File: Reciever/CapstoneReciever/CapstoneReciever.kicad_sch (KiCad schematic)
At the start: 44 parts, among them J1 Conn_01x04, Q1 CSD18502Q5B, Q2 CSD18502Q5B, U1 LM73606RNPR, U2 TPS552882RPMR, U3 ESP32-WROOM-32UE

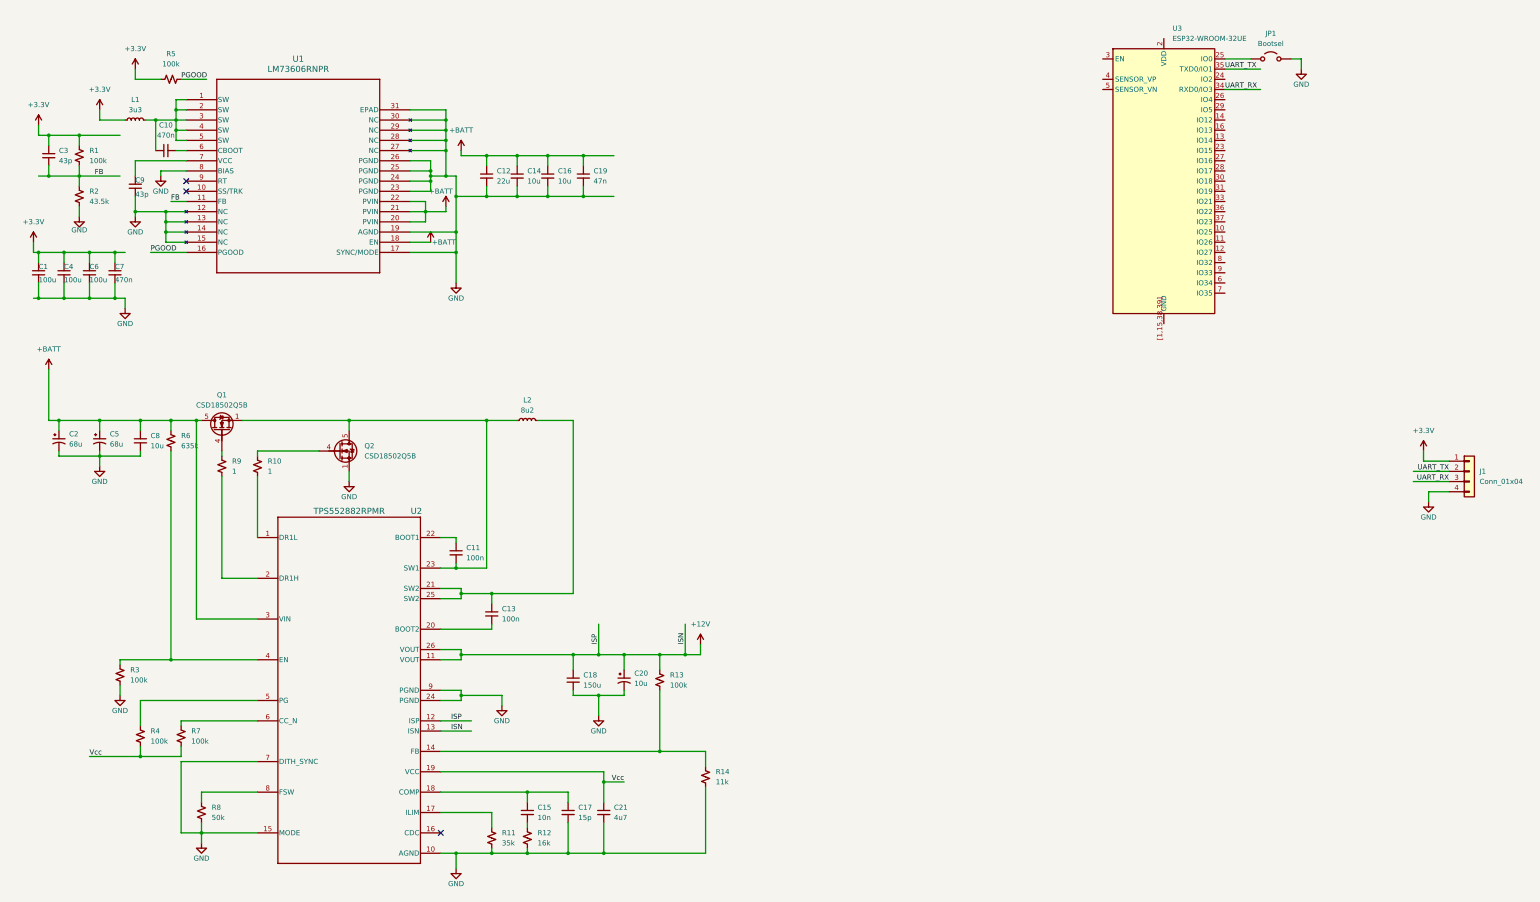
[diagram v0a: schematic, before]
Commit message: Finished ESP32 power and added in solenoid low side switching with TVS for coil transient protection
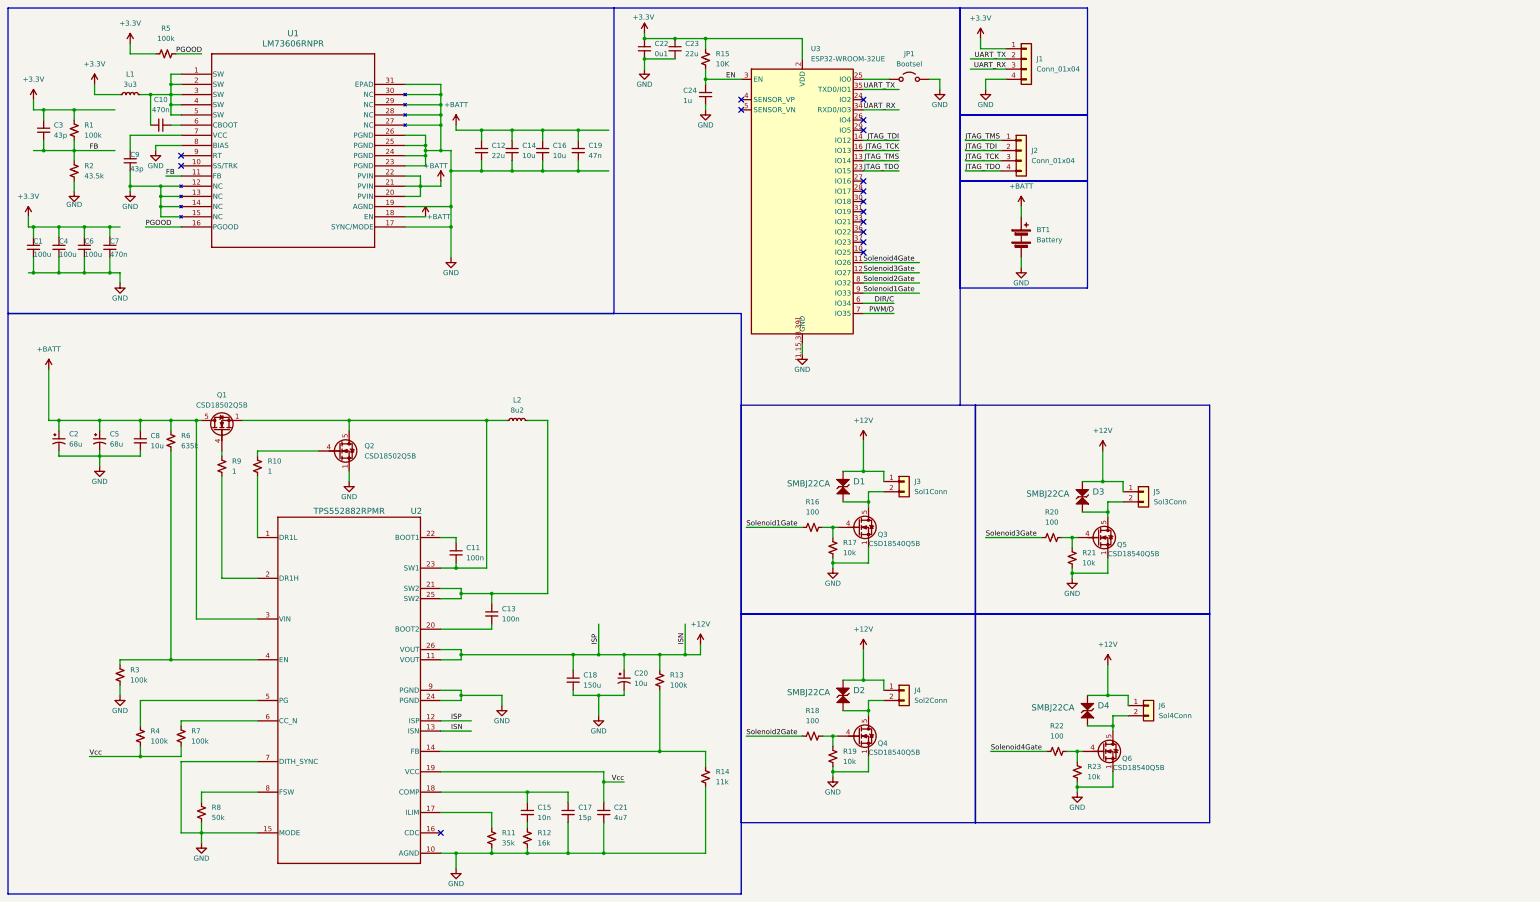
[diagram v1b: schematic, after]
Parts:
- added BT1: Battery, symbol Device:Battery
- added C22: 0u1, symbol Device:C_Small
- added C23: 22u, symbol Device:C_Small
- added C24: 1u, symbol Device:C_Small
- added D1, D2, D3, D4: ${DEVICE}, ICs And Semiconductors SMD:DIOM5336X265N, symbol CERN:Diodes/SMBJ22CA
- added J2: Conn_01x04, symbol Connector_Generic:Conn_01x04
- added J3: Sol1Conn, symbol Connector_Generic:Conn_01x02
- added J4: Sol2Conn, symbol Connector_Generic:Conn_01x02
- added J5: Sol3Conn, symbol Connector_Generic:Conn_01x02
- added J6: Sol4Conn, symbol Connector_Generic:Conn_01x02
- added Q3, Q4, Q5, Q6: CSD18540Q5B, Package_TO_SOT_SMD:TDSON-8-1, symbol Transistor_FET:CSD18540Q5B
- added R15: 10K, symbol Device:R_Small_US
- added R16, R18, R20, R22: 100, symbol Device:R_Small_US
- added R17, R19, R21, R23: 10k, symbol Device:R_Small_US
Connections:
- net +12V: now also D1.2, D2.2, D3.2, D4.2, J3.1 (Pin_1), J4.1 (Pin_1), J5.1 (Pin_1), J6.1 (Pin_1)
- net +3.3V: now also U3.2 (VDD), C22.1, C23.1, R15.1
- net +BATT: now also BT1.1 (+)
- net GND: now also U3.[1,15,38,39] (GND), BT1.2 (-), C22.2, C23.2, C24.2, Q3.1 (S), Q3.2 (S), Q3.3 (S), Q4.1 (S), Q4.2 (S), Q4.3 (S), Q5.1 (S), Q5.2 (S), Q5.3 (S), Q6.1 (S), Q6.2 (S), Q6.3 (S), R17.2, R19.2, R21.2, R23.2
- net Solenoid4Gate: now reaches U3.11 (IO26)
- net Solenoid4Gate: now also R22.1
- net Solenoid3Gate: now reaches U3.12 (IO27)
- net Solenoid3Gate: now also R20.1
- net JTAG_TMS: now reaches U3.13 (IO14)
- net JTAG_TMS: now also J2.1 (Pin_1)
- net JTAG_TDI: now reaches U3.14 (IO12)
- net JTAG_TDI: now also J2.2 (Pin_2)
- net JTAG_TCK: now reaches U3.16 (IO13)
- net JTAG_TCK: now also J2.3 (Pin_3)
- net JTAG_TDO: now reaches U3.23 (IO15)
- net JTAG_TDO: now also J2.4 (Pin_4)
- net EN: now reaches U3.3 (EN)
- net EN: now also C24.1, R15.2
- net DIR/C: now reaches U3.6 (IO34)
- net PWM/D: now reaches U3.7 (IO35)
- net Solenoid2Gate: now reaches U3.8 (IO32)
- net Solenoid2Gate: now also R18.1
- net Solenoid1Gate: now reaches U3.9 (IO33)
- net Solenoid1Gate: now also R16.1
- new net: Q3.4 (G), R16.2, R17.1
- new net: Q4.4 (G), R18.2, R19.1
- new net: D2.1, J4.2 (Pin_2), Q4.5 (D)
- new net: Q6.4 (G), R22.2, R23.1
- new net: D4.1, J6.2 (Pin_2), Q6.5 (D)
- new net: D1.1, J3.2 (Pin_2), Q3.5 (D)
- new net: D3.1, J5.2 (Pin_2), Q5.5 (D)
- new net: Q5.4 (G), R20.2, R21.1
- no-connect marks 3 -> 16
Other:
- moved on the sheet: C1, C10, C12, C14, C16, C19, C3, C4, C6, C7, C9, J1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

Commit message: Assigned footprints to components and moved them into the board editor
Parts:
- BT1, J3, J4, J5, J6: footprint (none) -> TerminalBlock_CUI:TerminalBlock_CUI_TB007-508-02_1x02_P5.08mm_Horizontal
- C1, C12, C14, C16, C18, C2, C20, C21, C23, C24, C4, C5, C6, C8, L1, L2: footprint (none) -> Capacitor_SMD:C_0603_1608Metric
- C10, C11, C13, C15, C17, C19, C22, C3, C7, C9: footprint (none) -> Capacitor_SMD:C_0402_1005Metric
- D1, D2, D3, D4: footprint ICs And Semiconductors SMD:DIOM5336X265N -> Diode_SMD:D_SMB
- J1, J2: footprint (none) -> Connector_PinHeader_2.54mm:PinHeader_1x04_P2.54mm_Vertical
- JP1: footprint (none) -> Connector_PinHeader_2.54mm:PinHeader_1x02_P2.54mm_Vertical
- R1, R10, R11, R12, R13, R14, R15, R16, R17, R18, R19, R2, R20, R21, R22, R23, R3, R4, R5, R6, R7, R8, R9: footprint (none) -> Resistor_SMD:R_0603_1608Metric
- U1: footprint RNP30_TEX -> footprints2:RNP30_TEX
- U2: footprint RPM0026A-MFG -> footprints2:RPM0026A-MFG
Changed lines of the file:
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@@
 			)
 		)
-		(property "Footprint" ""
+		(property "Footprint" "Capacitor_SMD:C_0603_1608Metric"
 			(at 152.4 179.07 0)
 			(hide yes)
@@
 			)
 		)
-		(property "Footprint" ""
+		(property "Footprint" "Resistor_SMD:R_0603_1608Metric"
 			(at 185.42 203.2 0)
 			(hide yes)
@@
 			)
 		)
-		(property "Footprint" ""
+		(property "Footprint" "Capacitor_SMD:C_0402_1005Metric"
 			(at 123.19 147.32 0)
 			(hide yes)
@@
 			)
 		)
-		(property "Footprint" "RNP30_TEX"
+		(property "Footprint" "footprints2:RNP30_TEX"
 			(at 54.61 27.94 0)
 			(hide yes)
@@
 			)
 		)
-		(property "Footprint" "RPM0026A-MFG"
+		(property "Footprint" "footprints2:RPM0026A-MFG"
 			(at 96.52 181.61 0)
 			(hide yes)
@@
 			)
 		)
-		(property "Footprint" ""
+		(property "Footprint" "Connector_PinHeader_2.54mm:PinHeader_1x02_P2.54mm_Vertical"
 			(at 236.22 29.21 0)
 			(hide yes)
@@
 			)
 		)
-		(property "Footprint" ""
+		(property "Footprint" "Resistor_SMD:R_0603_1608Metric"
 			(at 54.61 193.04 0)
 			(hide yes)
@@
 			)
 		)
-		(property "Footprint" ""
+		(property "Footprint" "Capacitor_SMD:C_0402_1005Metric"
 			(at 36.83 71.12 0)
 			(hide yes)
@@
 			)
 		)
-		(property "Footprint" ""
+		(property "Footprint" "Capacitor_SMD:C_0603_1608Metric"
 			(at 160.02 212.09 0)
 			(hide yes)
@@
 			)
 		)
-		(property "Footprint" ""
+		(property "Footprint" "Capacitor_SMD:C_0603_1608Metric"
 			(at 138.43 114.3 0)
 			(hide yes)
@@
 			)
 		)
-		(property "Footprint" ""
+		(property "Footprint" "Resistor_SMD:R_0603_1608Metric"
 			(at 217.17 146.05 0)
 			(hide yes)
@@
 			)
 		)
-		(property "Footprint" ""
+		(property "Footprint" "Capacitor_SMD:C_0603_1608Metric"
 			(at 137.16 46.99 0)
 			(hide yes)
@@
 			)
 		)
-		(property "Footprint" ""
+		(property "Footprint" "Resistor_SMD:R_0603_1608Metric"
 			(at 52.07 119.38 0)
 			(hide yes)
@@
 			)
 		)
-		(property "Footprint" ""
+		(property "Footprint" "Capacitor_SMD:C_0603_1608Metric"
 			(at 129.54 46.99 0)
 			(hide yes)
@@
 			)
 		)
-		(property "Footprint" ""
+		(property "Footprint" "TerminalBlock_CUI:TerminalBlock_CUI_TB007-508-02_1x02_P5.08mm_Horizontal"
 			(at 234.95 181.61 0)
 			(hide yes)
@@
 			)
 		)
-		(property "Footprint" ""
+		(property "Footprint" "Capacitor_SMD:C_0402_1005Metric"
 			(at 20.32 41.91 0)
 			(hide yes)
@@
 			)
 		)
-		(property "Footprint" ""
+		(property "Footprint" "Capacitor_SMD:C_0603_1608Metric"
 			(at 185.42 33.02 0)
 			(hide yes)
@@
 			)
 		)
-		(property "Footprint" ""
+		(property "Footprint" "Capacitor_SMD:C_0402_1005Metric"
 			(at 170.18 21.59 0)
 			(hide yes)
@@
 			)
 		)
-		(property "Footprint" ""
+		(property "Footprint" "Resistor_SMD:R_0603_1608Metric"
 			(at 27.94 41.91 0)
 			(hide yes)
@@
 			)
 		)
-		(property "Footprint" ""
+		(property "Footprint" "Resistor_SMD:R_0603_1608Metric"
 			(at 44.45 193.04 0)
 			(hide yes)
@@
 			)
 		)
-		(property "Footprint" ""
+		(property "Footprint" "Resistor_SMD:R_0603_1608Metric"
 			(at 64.77 125.73 0)
 			(hide yes)
@@
 			)
 		)
-		(property "Footprint" ""
+		(property "Footprint" "Capacitor_SMD:C_0402_1005Metric"
 			(at 153.67 46.99 0)
 			(hide yes)
@@
 			)
 		)
-		(property "Footprint" "ICs And Semiconductors SMD:DIOM5336X265N"
+		(property "Footprint" "Diode_SMD:D_SMB"
 			(at 219.71 186.69 0)
 			(hide yes)
@@
 			)
 		)
-		(property "Footprint" ""
+		(property "Footprint" "Capacitor_SMD:C_0603_1608Metric"
 			(at 165.1 179.07 0)
 			(hide yes)
@@
 			)
 		)
-		(property "Footprint" ""
+		(property "Footprint" "Capacitor_SMD:C_0402_1005Metric"
 			(at 140.97 212.09 0)
 			(hide yes)
@@
 			)
 		)
-		(property "Footprint" "ICs And Semiconductors SMD:DIOM5336X265N"
+		(property "Footprint" "Diode_SMD:D_SMB"
 			(at 219.71 134.62 0)
 			(hide yes)
@@
 			)
 		)
-		(property "Footprint" ""
+		(property "Footprint" "Resistor_SMD:R_0603_1608Metric"
 			(at 132.08 218.44 0)
 			(hide yes)
@@
 			)
 		)
-		(property "Footprint" ""
+		(property "Footprint" "TerminalBlock_CUI:TerminalBlock_CUI_TB007-508-02_1x02_P5.08mm_Horizontal"
 			(at 294.64 132.08 0)
 			(hide yes)
@@
 			)
 		)
-		(property "Footprint" ""
+		(property "Footprint" "Connector_PinHeader_2.54mm:PinHeader_1x04_P2.54mm_Vertical"
 			(at 264.16 46.99 0)
 			(hide yes)
@@
 			)
 		)
-		(property "Footprint" ""
+		(property "Footprint" "Capacitor_SMD:C_0603_1608Metric"
 			(at 24.13 71.12 0)
 			(hide yes)
@@
 			)
 		)
-		(property "Footprint" ""
+		(property "Footprint" "Capacitor_SMD:C_0603_1608Metric"
 			(at 17.78 71.12 0)
 			(hide yes)
@@
 			)
 		)
-		(property "Footprint" ""
+		(property "Footprint" "Resistor_SMD:R_0603_1608Metric"
 			(at 212.09 193.04 0)
 			(hide yes)
@@
 			)
 		)
-		(property "Footprint" "ICs And Semiconductors SMD:DIOM5336X265N"
+		(property "Footprint" "Diode_SMD:D_SMB"
 			(at 279.4 137.16 0)
 			(hide yes)
@@
 			)
 		)
-		(property "Footprint" ""
+		(property "Footprint" "Resistor_SMD:R_0603_1608Metric"
 			(at 27.94 52.07 0)
 			(hide yes)
@@
 			)
 		)
-		(property "Footprint" ""
+		(property "Footprint" "Resistor_SMD:R_0603_1608Metric"
 			(at 59.69 212.09 0)
 			(hide yes)
@@
 			)
 		)
-		(property "Footprint" ""
+		(property "Footprint" "Capacitor_SMD:C_0402_1005Metric"
 			(at 132.08 162.56 0)
 			(hide yes)
@@
 			)
 		)
-		(property "Footprint" ""
+		(property "Footprint" "Resistor_SMD:R_0603_1608Metric"
 			(at 273.05 196.85 0)
 			(hide yes)
@@
 			)
 		)
-		(property "Footprint" ""
+		(property "Footprint" "Resistor_SMD:R_0603_1608Metric"
 			(at 212.09 140.97 0)
 			(hide yes)
@@
 			)
 		)
-		(property "Footprint" ""
+		(property "Footprint" "Capacitor_SMD:C_0603_1608Metric"
 			(at 34.29 119.38 0)
 			(hide yes)
@@
 			)
 		)
-		(property "Footprint" ""
+		(property "Footprint" "Capacitor_SMD:C_0402_1005Metric"
 			(at 151.13 212.09 0)
 			(hide yes)
@@
 			)
 		)
-		(property "Footprint" ""
+		(property "Footprint" "Resistor_SMD:R_0603_1608Metric"
 			(at 140.97 218.44 0)
 			(hide yes)
@@
 			)
 		)
-		(property "Footprint" ""
+		(property "Footprint" "Resistor_SMD:R_0603_1608Metric"
 			(at 271.78 143.51 0)
 			(hide yes)
@@
 			)
 		)
-		(property "Footprint" ""
+		(property "Footprint" "Capacitor_SMD:C_0402_1005Metric"
 			(at 41.91 49.53 0)
 			(hide yes)
@@
 			)
 		)
-		(property "Footprint" ""
+		(property "Footprint" "Resistor_SMD:R_0603_1608Metric"
 			(at 39.37 177.8 0)
 			(hide yes)
@@
 			)
 		)
-		(property "Footprint" ""
+		(property "Footprint" "Capacitor_SMD:C_0603_1608Metric"
 			(at 24.13 119.38 0)
 			(hide yes)
@@
 			)
 		)
-		(property "Footprint" "ICs And Semiconductors SMD:DIOM5336X265N"
+		(property "Footprint" "Diode_SMD:D_SMB"
 			(at 280.67 190.5 0)
 			(hide yes)
@@
 			)
 		)
-		(property "Footprint" ""
+		(property "Footprint" "Capacitor_SMD:C_0603_1608Metric"
 			(at 144.78 46.99 0)
 			(hide yes)
@@
 			)
 		)
-		(property "Footprint" ""
+		(property "Footprint" "Capacitor_SMD:C_0603_1608Metric"
 			(at 44.45 119.38 0)
 			(hide yes)
@@
 			)
 		)
-		(property "Footprint" ""
+		(property "Footprint" "Resistor_SMD:R_0603_1608Metric"
 			(at 173.99 179.07 0)
 			(hide yes)
@@
 			)
 		)
-		(property "Footprint" ""
+		(property "Footprint" "Capacitor_SMD:C_0603_1608Metric"
 			(at 41.91 33.02 0)
 			(hide yes)
@@
 			)
 		)
-		(property "Footprint" ""
+		(property "Footprint" "Resistor_SMD:R_0603_1608Metric"
 			(at 217.17 198.12 0)
 			(hide yes)
@@
 			)
 		)
-		(property "Footprint" ""
+		(property "Footprint" "TerminalBlock_CUI:TerminalBlock_CUI_TB007-508-02_1x02_P5.08mm_Horizontal"
 			(at 295.91 185.42 0)
 			(hide yes)
@@
 			)
 		)
-		(property "Footprint" ""
+		(property "Footprint" "Resistor_SMD:R_0603_1608Metric"
 			(at 185.42 24.13 0)
 			(hide yes)
@@
 			)
 		)
-		(property "Footprint" ""
+		(property "Footprint" "Resistor_SMD:R_0603_1608Metric"
 			(at 276.86 148.59 0)
 			(hide yes)
@@
 			)
 		)
-		(property "Footprint" ""
+		(property "Footprint" "Capacitor_SMD:C_0603_1608Metric"
 			(at 177.8 21.59 0)
 			(hide yes)
@@
 			)
 		)
-		(property "Footprint" ""
+		(property "Footprint" "Connector_PinHeader_2.54mm:PinHeader_1x04_P2.54mm_Vertical"
 			(at 265.43 24.13 0)
 			(hide yes)
@@
 			)
 		)
-		(property "Footprint" ""
+		(property "Footprint" "TerminalBlock_CUI:TerminalBlock_CUI_TB007-508-02_1x02_P5.08mm_Horizontal"
 			(at 234.95 129.54 0)
 			(hide yes)
@@
 			)
 		)
-		(property "Footprint" ""
+		(property "Footprint" "Resistor_SMD:R_0603_1608Metric"
 			(at 278.13 201.93 0)
 			(hide yes)
@@
 			)
 		)
-		(property "Footprint" ""
+		(property "Footprint" "TerminalBlock_CUI:TerminalBlock_CUI_TB007-508-02_1x02_P5.08mm_Horizontal"
 			(at 264.16 67.056 90)
 			(hide yes)
@@
 			)
 		)
-		(property "Footprint" ""
+		(property "Footprint" "Capacitor_SMD:C_0603_1608Metric"
 			(at 30.48 71.12 0)
 			(hide yes)
@@
 			)
 		)
-		(property "Footprint" ""
+		(property "Footprint" "Resistor_SMD:R_0603_1608Metric"
 			(at 50.8 22.86 0)
 			(hide yes)
@@
 			)
 		)
-		(property "Footprint" ""
+		(property "Footprint" "Capacitor_SMD:C_0402_1005Metric"
 			(at 49.53 40.64 0)
 			(hide yes)
@@
 			)
 		)
-		(property "Footprint" ""
+		(property "Footprint" "Resistor_SMD:R_0603_1608Metric"
 			(at 73.66 125.73 0)
 			(hide yes)

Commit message: Added more descriptive net names and routed low side switching mosfets with ESP32 decoupling
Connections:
- net Solenoid1Gate: now also U3.8 (IO32); no longer U3.9 (IO33)
- net Solenoid2Gate: now also U3.9 (IO33); no longer U3.8 (IO32)
- net Solenoid3Gate: now also U3.11 (IO26); no longer U3.12 (IO27)
- net Solenoid4Gate: now also U3.12 (IO27); no longer U3.11 (IO26)
- net Q3Gate: now reaches Q3.4 (G), R16.2, R17.1
- net Q4Gate: now reaches Q4.4 (G), R18.2, R19.1
- net Q4Drain: now reaches D2.1, J4.2 (Pin_2), Q4.5 (D)
- net Q6Gate: now reaches Q6.4 (G), R22.2, R23.1
- net Q6Drain: now reaches D4.1, J6.2 (Pin_2), Q6.5 (D)
- net Q3Drain: now reaches D1.1, J3.2 (Pin_2), Q3.5 (D)
- net Q5Drain: now reaches D3.1, J5.2 (Pin_2), Q5.5 (D)
- net Q5Gate: now reaches Q5.4 (G), R20.2, R21.1
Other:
- moved on the sheet: R17

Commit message: Attempted to work on power routing. Stuck. Please assist
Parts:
- removed C20: 10u, Capacitor_SMD:C_0603_1608Metric, symbol Device:C_Polarized_Small_US
- added C20: 10u, Capacitor_SMD:C_0603_1608Metric, symbol Device:C_Small
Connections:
- net +12V: now also C20.1
- net GND: now also C20.2
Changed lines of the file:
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@@
 	)
 	(symbol
+		(lib_id "Device:C_Small")
+		(at 165.1 179.07 0)
+		(unit 1)
+		(body_style 1)
+		(exclude_from_sim no)
+		(in_bom yes)
+		(on_board yes)
+		(in_pos_files yes)
+		(dnp no)
+		(fields_autoplaced yes)
+		(property "Reference" "C20"
+			(at 167.64 177.8062 0)
+			(show_name no)
+			(do_not_autoplace no)
+			(effects
+				(font
+					(size 1.27 1.27)
+				)
+				(justify left)
+			)
+		)
+		(property "Value" "10u"
+			(at 167.64 180.3462 0)
+			(show_name no)
+			(do_not_autoplace no)
+			(effects
+				(font
+					(size 1.27 1.27)
+				)
+				(justify left)
+			)
+		)
+		(property "Footprint" "Capacitor_SMD:C_0603_1608Metric"
+			(at 165.1 179.07 0)
+			(hide yes)
+			(show_name no)
+			(do_not_autoplace no)
+			(effects
+				(font
+					(size 1.27 1.27)
+				)
+			)
+		)
+		(property "Datasheet" ""
+			(at 165.1 179.07 0)
+			(hide yes)
+			(show_name no)
+			(do_not_autoplace no)
+			(effects
+				(font
+					(size 1.27 1.27)
+				)
+			)
+		)
+		(property "Description" "Unpolarized capacitor, small symbol"
+			(at 165.1 179.07 0)
+			(hide yes)
+			(show_name no)
+			(do_not_autoplace no)
+			(effects
+				(font
+					(size 1.27 1.27)
+				)
+			)
+		)
+		(pin "1"
+		)
+		(pin "2"
+		)
+		(instances
+			(project "CapstoneReciever"
+				(path "/42a8ff87-24fb-42f5-a20d-20469faac78a"
+					(reference "C20")
+					(unit 1)
+				)
+			)
+		)
+	)
+	(symbol
 		(lib_id "power:+BATT")
 		(at 21.59 101.6 0)
@@
 					(unit 1)
 				)
-			)
-		)
-	)
-	(symbol
-		(lib_id "Device:C_Polarized_Small_US")
-		(at 165.1 179.07 0)
-		(unit 1)
-		(body_style 1)
-		(exclude_from_sim no)
-		(in_bom yes)
-		(on_board yes)
-		(in_pos_files yes)
-		(dnp no)
-		(fields_autoplaced yes)
-		(property "Reference" "C20"
-			(at 167.64 177.3681 0)
-			(show_name no)
-			(do_not_autoplace no)
-			(effects
-				(font
-					(size 1.27 1.27)
-				)
-				(justify left)
-			)
-		)
-		(property "Value" "10u"
-			(at 167.64 179.9081 0)
-			(show_name no)
-			(do_not_autoplace no)
-			(effects
-				(font
-					(size 1.27 1.27)
-				)
-				(justify left)
-			)
-		)
-		(property "Footprint" "Capacitor_SMD:C_0603_1608Metric"
-			(at 165.1 179.07 0)
-			(hide yes)
-			(show_name no)
-			(do_not_autoplace no)
-			(effects
-				(font
-					(size 1.27 1.27)
-				)
-			)
-		)
-		(property "Datasheet" ""
-			(at 165.1 179.07 0)
-			(hide yes)
-			(show_name no)
-			(do_not_autoplace no)
-			(effects
-				(font
-					(size 1.27 1.27)
-				)
-			)
-		)
-		(property "Description" "Polarized capacitor, small US symbol"
-			(at 165.1 179.07 0)
-			(hide yes)
-			(show_name no)
-			(do_not_autoplace no)
-			(effects
-				(font
-					(size 1.27 1.27)
-				)
-			)
-		)
-		(pin "2"
-		)
-		(pin "1"
-		)
-		(instances
-			(project "CapstoneReciever"
-				(path "/42a8ff87-24fb-42f5-a20d-20469faac78a"
-					(reference "C20")
-					(unit 1)
-				)
